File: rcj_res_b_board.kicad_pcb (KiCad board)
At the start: 2 copper layers, 90 x 100 mm, 76 parts, among them P1 CONN_01X02, P10 PING0, P11 MPU9250, P12 SERVO0, P13 CONN_01X04, P14 CONN_01X03, P15 CONN_01X03, P2 CONN_01X02, P3 GP2Y0A41SK0F, P4 GP2Y0A41SK0F, P5 GP2Y0A41SK0F, P6 GP2Y0A41SK0F, P7 GP2Y0A21YK, P8 GP2Y0A21YK, P9 GP2Y0A21YK, U1 OPB733TR

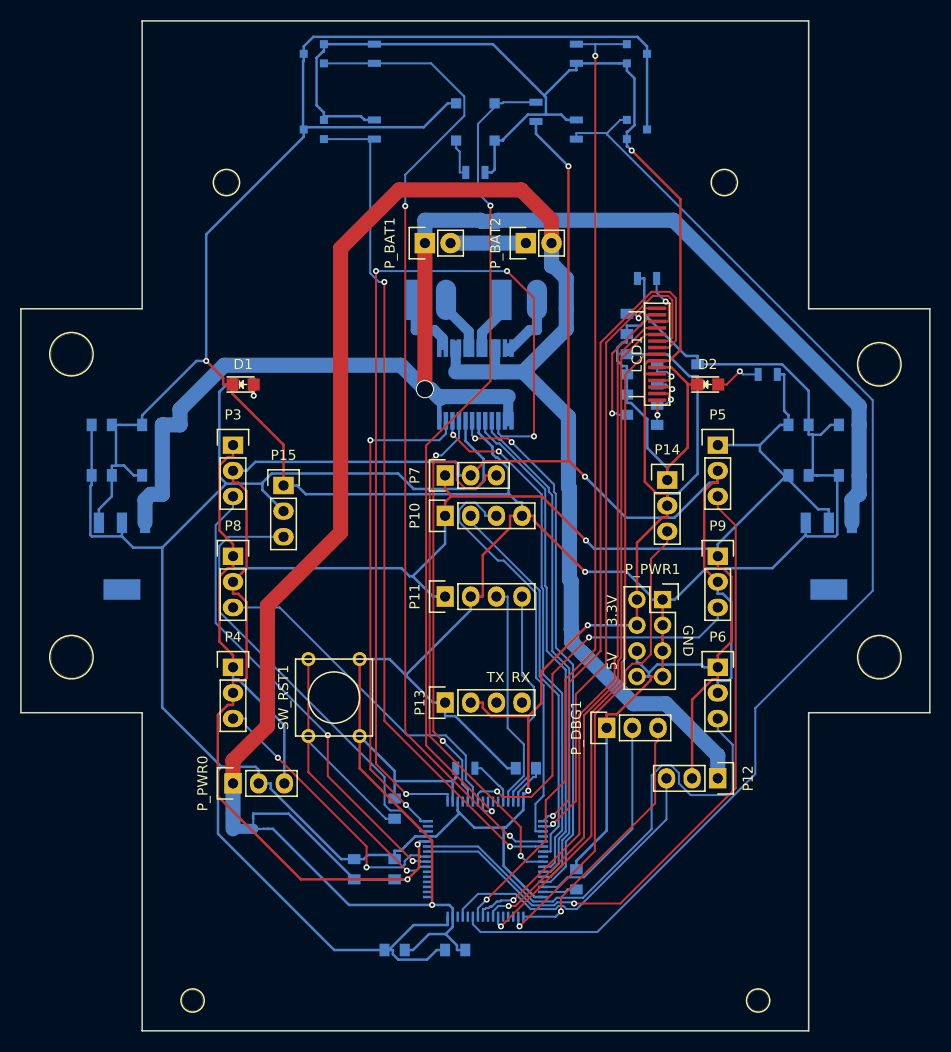
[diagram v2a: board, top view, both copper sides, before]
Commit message: Prep for fabrication
Added ground planes
Added switches
Added cutoffs for mounting sensors
Added additional silkscreen info
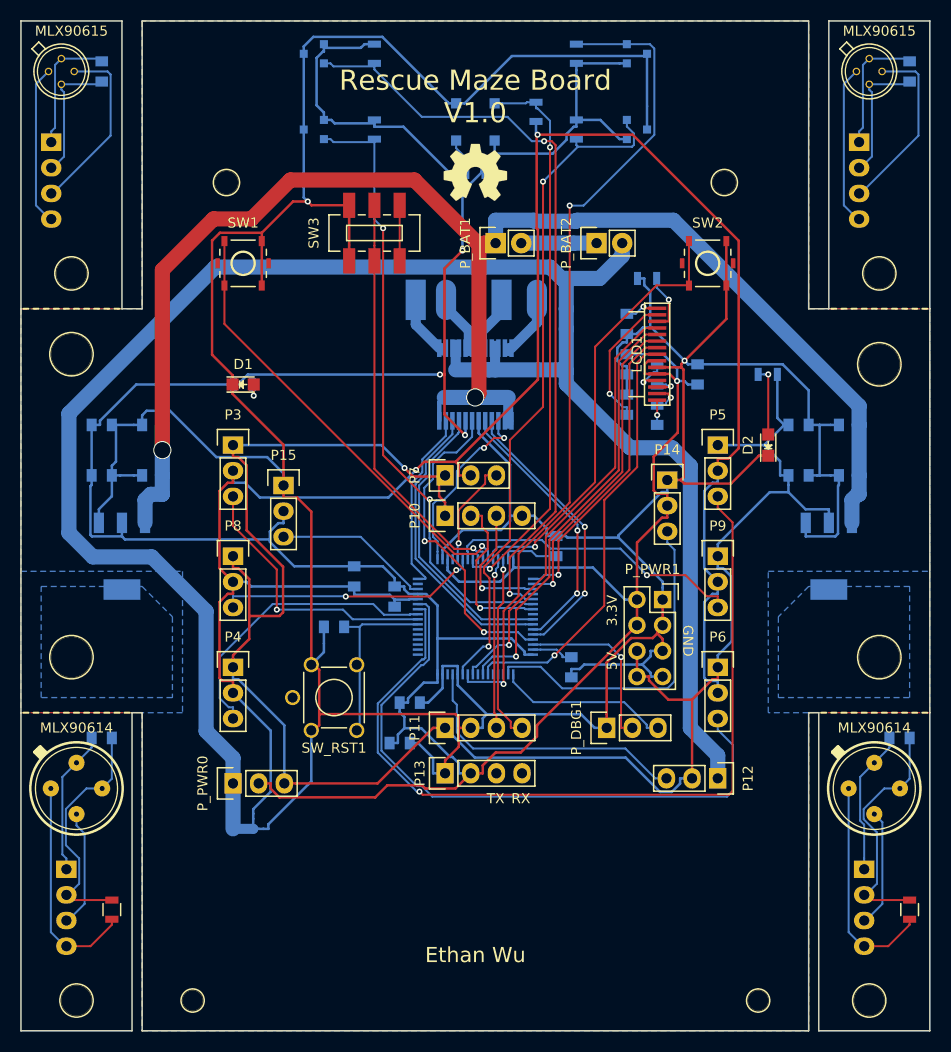
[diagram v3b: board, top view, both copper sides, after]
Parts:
- removed the R1 at (64.0, 124.0)
- added C_CT0_1: 0.1uF, Capacitors_SMD:C_0805, B.Cu at (28.0, 121.0)
- added C_CT0_2: 0.1uF, Capacitors_SMD:C_0805, B.Cu at (107.0, 121.0)
- added C_CT0_3: 0.1uF, Capacitors_SMD:C_0805, B.Cu at (28.0, 55.0)
- added C_CT0_4: 0.1uF, Capacitors_SMD:C_0805, B.Cu at (108.0, 55.0)
- added G001: LOGO, Custom:OSH_LOGO, F.Cu at (65.0, 65.0)
- added HOLE7: 1pin, Connect:1pin, F.Cu at (104.0, 147.0)
- added HOLE7: 1pin, Connect:1pin, F.Cu at (25.5, 147.0)
- added HOLE8: 1pin, Connect:1pin, F.Cu at (25.0, 75.0)
- added HOLE9: 1pin, Connect:1pin, F.Cu at (105.0, 75.0)
- added P16: CONN_01X04, Socket_Strips:Socket_Strip_Straight_1x04, B.Cu at (24.5, 134.0)
- added P17: CONN_01X04, Socket_Strips:Socket_Strip_Straight_1x04, B.Cu at (103.5, 134.0)
- added P18: CONN_01X04, Socket_Strips:Socket_Strip_Straight_1x04, B.Cu at (23.0, 62.0)
- added P19: CONN_01X04, Socket_Strips:Socket_Strip_Straight_1x04, B.Cu at (103.0, 62.0)
- added R_CT0_1: 10k, Resistors_SMD:R_0805, F.Cu at (29.0, 138.0)
- added R_CT0_2: 10k, Resistors_SMD:R_0805, F.Cu at (108.0, 138.0)
- added SW1: SW_PUSH, Custom:EVQPL, F.Cu at (42.0, 74.0)
- added SW2: SW_PUSH, Custom:EVQPL, F.Cu at (88.0, 74.0)
- added SW3: SWITCH_INV, Custom:JS202011SCQN, F.Cu at (55.0, 71.0)
- added U_CT0_1: MLX90614, Custom:TO-39, F.Cu at (25.5, 126.0)
- added U_CT0_2: MLX90614, Custom:TO-39, F.Cu at (104.5, 126.0)
- added U_CT0_3: MLX90615, Custom:TO-46_4Pin, F.Cu at (24.0, 55.0)
- added U_CT0_4: MLX90615, Custom:TO-46_4Pin, F.Cu at (104.0, 55.0)
- C10, C13: value 4.7uF -> 10uF
- C14, C15, C18, C19: value 2.2uF -> 10uF
- C9: value 103p -> 0.01uF
- P_BAT1, P_BAT2: footprint Socket_Strips:Socket_Strip_Straight_1x02 -> Pin_Headers:Pin_Header_Straight_1x02
- SW_RST1: footprint Buttons_Switches_ThroughHole:SW_PUSH_SMALL -> Custom:EVQPB
- moved C11 29.0 mm to (53.0, 105.0)
- moved C10 27.0 mm to (57.0, 107.0)
- moved C13 24.5 mm to (58.5, 117.5)
- moved MCU1 24.0 mm to (65.0, 109.0)
- moved C15 22.2 mm to (73.0, 102.0), turned to 90 degrees
- moved C12 21.2 mm to (57.5, 121.5)
- moved C14 21.0 mm to (74.5, 114.0), turned to 270 degrees
- moved C9 19.0 mm to (51.0, 110.0), turned to 180 degrees
- moved P11 13.0 mm to (62.0, 120.0)
- moved D2 8.49 mm to (94.0, 92.0), turned to 90 degrees
- moved P13 7.00 mm to (62.0, 124.5)
- moved P_BAT1 7.00 mm to (67.0, 72.0), turned to 90 degrees
- moved P_BAT2 7.00 mm to (77.0, 72.0), turned to 90 degrees
- turned SW_RST1 to 180 degrees
- renumbered R2 to R1, R3 to R2, R4 to R3, R5 to R4, R6 to R5, R7 to R6, R8 to R7, R9 to R8, R10 to R9
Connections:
- MCU1 pad 26: Net-(MCU1-Pad26) -> /MODE_SEL
- MCU1 pad 27: Net-(MCU1-Pad27) -> /USR1
- MCU1 pad 28: Net-(MCU1-Pad28) -> /USR2
- MCU1 pad 60: Net-(MCU1-Pad60) -> GNDD
- REG1 pad 4: (no net) -> Net-(REG1-Pad4)
- REG2 pad 4: (no net) -> Net-(REG2-Pad4)
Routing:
- net /MD_BPWM: track 93.2 -> 18.3 mm, vias 4 -> 2
- net /M1_ENC_B: track 120.8 -> 66.9 mm, vias 0 -> 2
- net /USR1: track 0.00 -> 45.2 mm, vias 0 -> 1
- net /3.3V: track 376.0 -> 332.0 mm, vias 3 -> 4
- net /USR2: track 0.00 -> 43.6 mm, vias 0 -> 1
- net /MODE_SEL: track 0.00 -> 41.1 mm, vias 0 -> 1
- net /OLED_RST: track 66.2 -> 29.9 mm
- net /OLED_D-C: track 64.9 -> 31.0 mm
- net /IR_L_F: track 44.0 -> 10.5 mm
- net /MD_APWM: track 49.5 -> 18.4 mm, vias 2 -> 0
- net /TEMP1_PWM: track 44.6 -> 15.6 mm
- net /PING0_ECHO: track 41.4 -> 13.0 mm, vias 0 -> 1
- net /LS_FLOOR: track 82.6 -> 56.0 mm
- net Net-(C_CT0_2-Pad1): track 0.00 -> 24.2 mm
- net Net-(C_CT0_1-Pad1): track 0.00 -> 24.2 mm
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- added copper zone on B.Cu, net GNDD
- added copper zone on F.Cu, net GNDD
- added copper zone on B.Cu, net Net-(REG1-Pad4)
- added copper zone on B.Cu, net Net-(REG2-Pad4)
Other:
- outline, holes or cut-outs redrawn
- board text added: "0.1uF"
- board text added: "Ethan Wu"
- board text added: "MLX90614"
- board text added: "MLX90615"
- board text added: "Rescue Maze Board V1.0"
- board text added: "SCL"
- board text added: "SDA"
- board text added: "VCC"

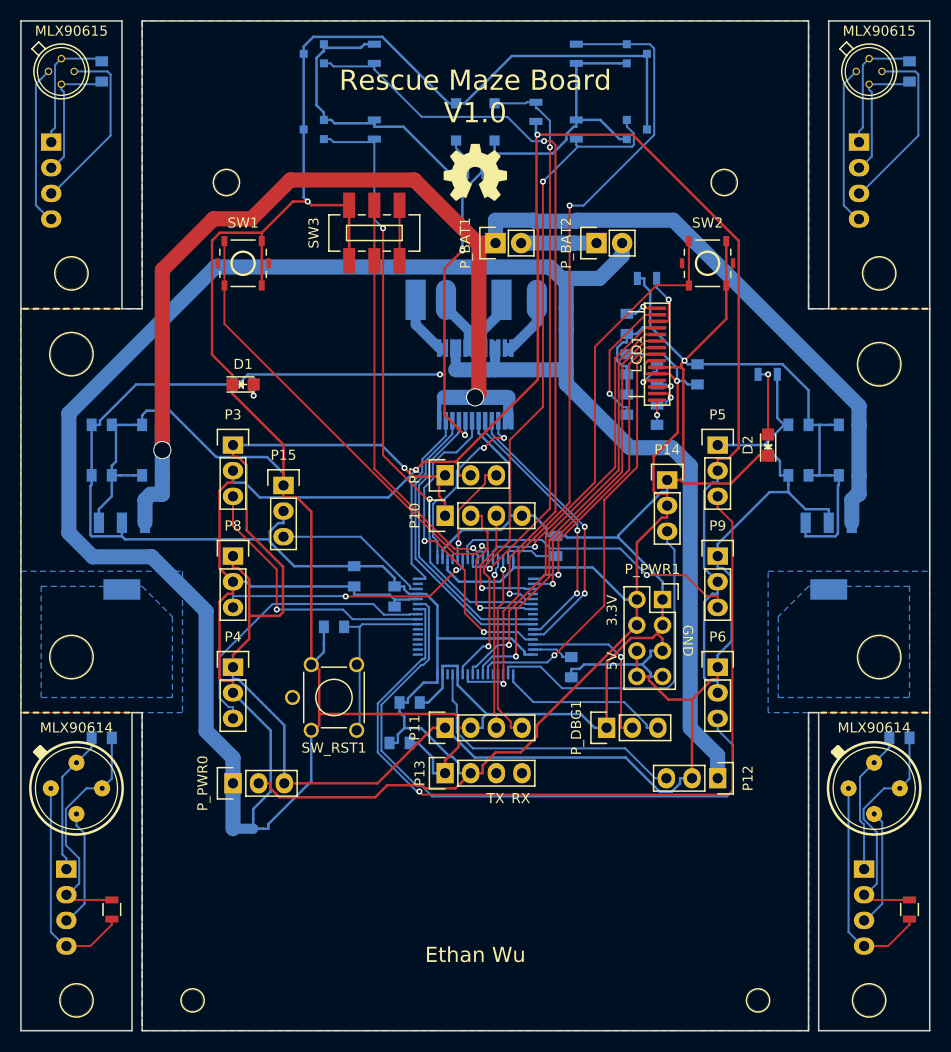
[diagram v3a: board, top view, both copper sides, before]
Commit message: Minor fixes
Connected previously disconnected serial port (in schematic)
Added labels
Added missing cutout in side of board
Adjusted mounting hole positions
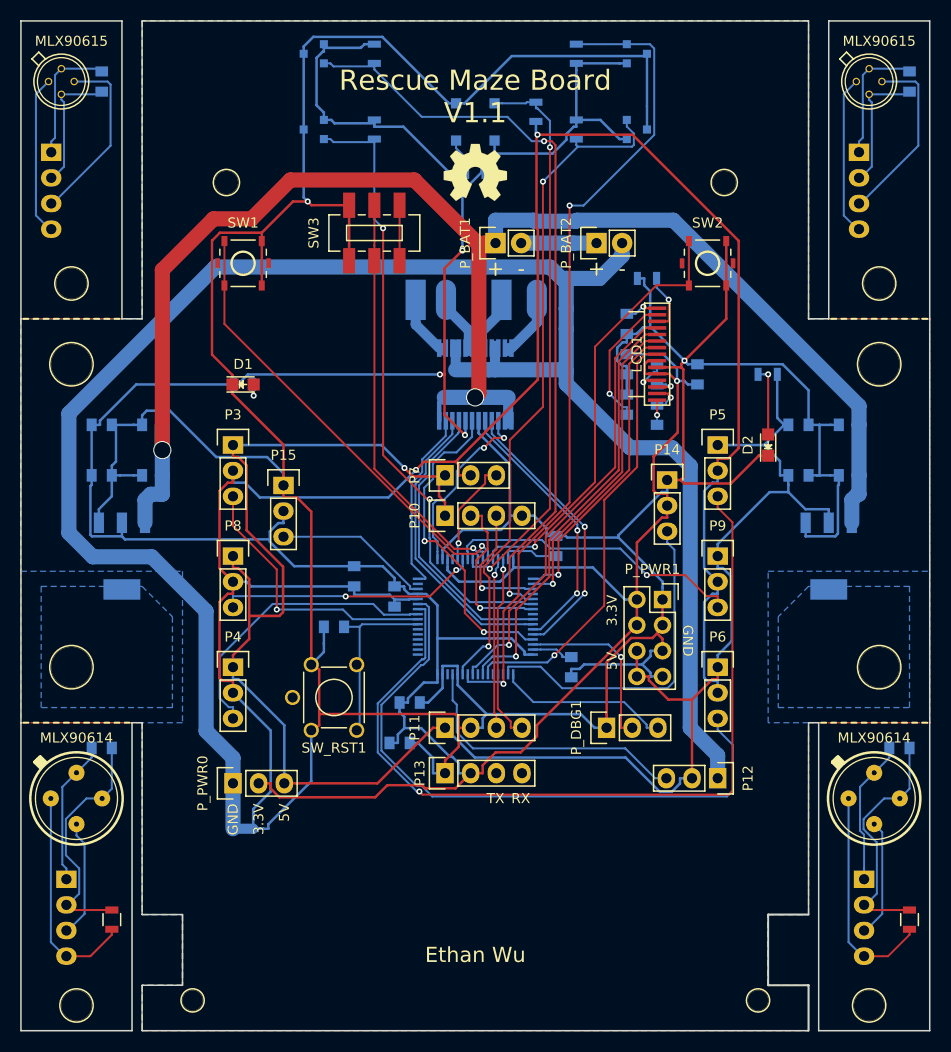
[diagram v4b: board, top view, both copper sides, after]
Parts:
- moved C_CT0_1 1.00 mm to (28.0, 122.0)
- moved C_CT0_2 1.00 mm to (107.0, 122.0)
- moved C_CT0_3 1.00 mm to (28.0, 56.0)
- moved C_CT0_4 1.00 mm to (108.0, 56.0)
- moved HOLE1 1.00 mm to (25.0, 84.0)
- moved HOLE2 1.00 mm to (25.0, 114.0)
- moved HOLE4 1.00 mm to (105.0, 114.0)
- moved HOLE8 1.00 mm to (25.0, 76.0)
- moved HOLE9 1.00 mm to (105.0, 76.0)
- moved P16 1.00 mm to (24.5, 135.0)
- moved P17 1.00 mm to (103.5, 135.0)
- moved P18 1.00 mm to (23.0, 63.0)
- moved P19 1.00 mm to (103.0, 63.0)
- moved R_CT0_1 1.00 mm to (29.0, 139.0)
- moved R_CT0_2 1.00 mm to (108.0, 139.0)
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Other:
- outline, holes or cut-outs redrawn
- board text added: "+"
- board text added: "-"
- board text added: "Rescue Maze Board V1.1"
- board text removed: "Rescue Maze Board V1.0"

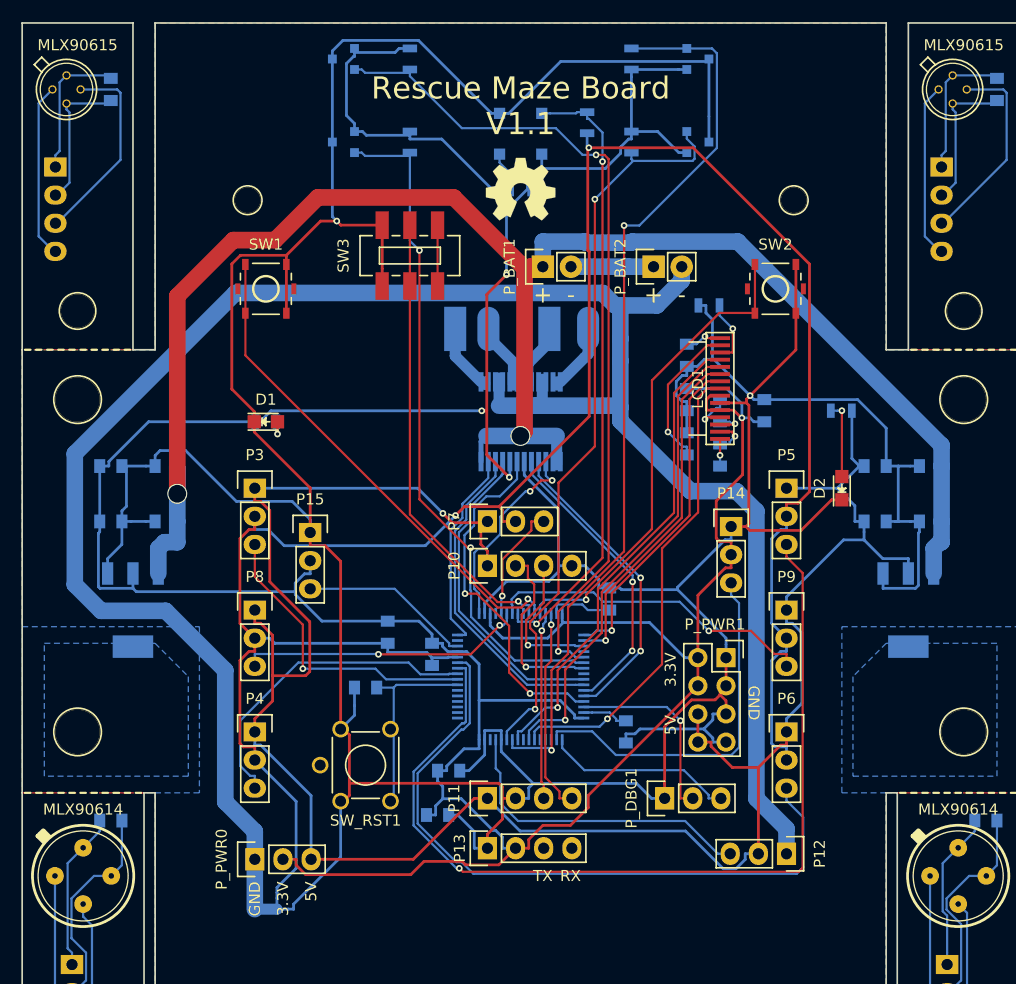
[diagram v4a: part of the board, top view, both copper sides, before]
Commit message: Moved hall-effect sensors
Connected serial port in netlist (netlist update)
Added pcbnew autosaves to gitignore
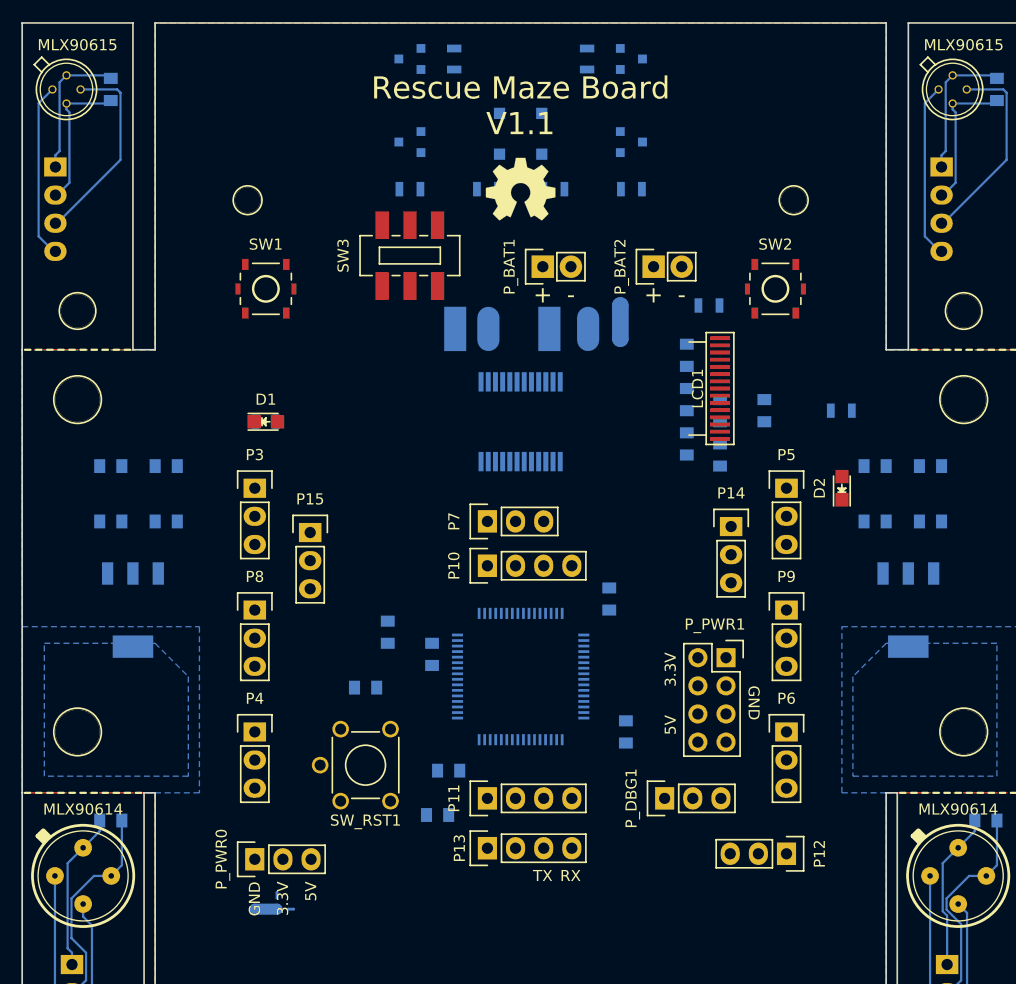
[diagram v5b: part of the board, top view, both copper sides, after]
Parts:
- moved R8 6.71 mm to (68.0, 65.0), turned to 0 degrees
- moved HAL_M0A1 6.00 mm to (55.0, 53.2)
- moved HAL_M0B1 6.00 mm to (55.0, 60.8)
- moved HAL_M1A1 6.00 mm to (75.0, 53.2)
- moved HAL_M1B1 6.00 mm to (75.0, 60.8)
- moved R4 4.25 mm to (55.0, 65.0), turned to 0 degrees
- moved R6 4.25 mm to (75.0, 65.0), turned to 0 degrees
- moved R3 4.00 mm to (59.0, 53.2)
- moved R5 4.00 mm to (71.0, 53.2)
- moved R7 3.00 mm to (62.0, 65.0)
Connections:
- MCU1 pad 51: Net-(MCU1-Pad51) -> /UART_TX
- MCU1 pad 52: Net-(MCU1-Pad52) -> /UART_RX
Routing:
- net GNDD: track 426.2 -> 0.00 mm, vias 2 -> 0
- net /3.3V: track 332.0 -> 0.00 mm, vias 4 -> 0
- net GNDA: track 199.1 -> 0.00 mm, vias 2 -> 0
- net /5V: track 191.3 -> 0.00 mm, vias 1 -> 0
- net VCC: track 153.8 -> 0.00 mm, vias 2 -> 0
- net GND: track 114.7 -> 0.00 mm
- net /IR_S_RF: track 83.8 -> 0.00 mm, vias 1 -> 0
- net /M1_ENC_A: track 82.2 -> 0.00 mm, vias 2 -> 0
- net /M0_ENC_A: track 75.6 -> 0.00 mm, vias 2 -> 0
- net GNDPWR: track 72.9 -> 0.00 mm
- net /M1_ENC_B: track 66.9 -> 0.00 mm, vias 2 -> 0
- net /IR_S_RB: track 62.2 -> 0.00 mm
- net /M0_ENC_B: track 61.4 -> 0.00 mm, vias 2 -> 0
- net /LS_FLOOR: track 56.0 -> 0.00 mm, vias 2 -> 0
- net /USR1: track 45.2 -> 0.00 mm, vias 1 -> 0
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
